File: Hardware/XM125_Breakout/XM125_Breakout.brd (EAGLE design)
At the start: 25.4 x 50.8 mm, 82 parts, among them J2 QWIIC_RIGHT_ANGLE, J3 QWIIC_RIGHT_ANGLE, U1 XM125, U2 RT9080-33GJ5, U3 RT9080-18GJ5, U4 CH340C, U5 ESD Diode

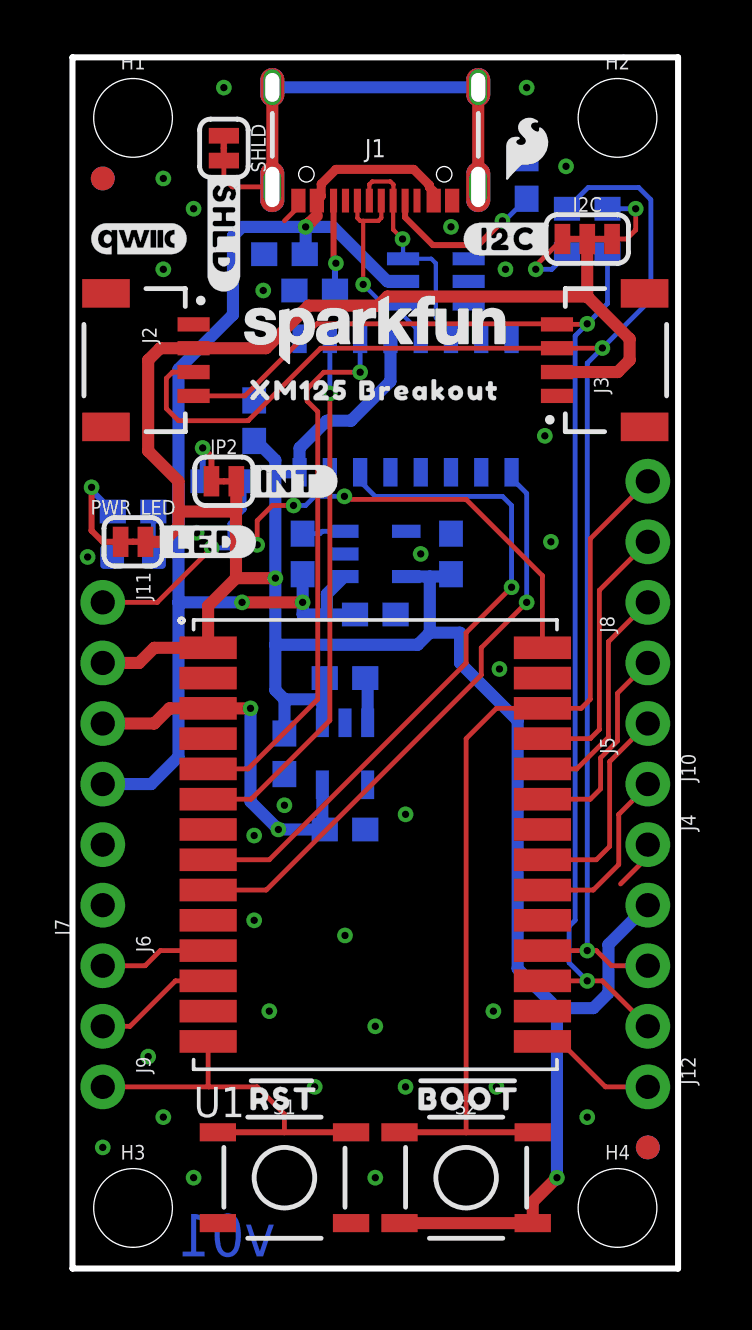
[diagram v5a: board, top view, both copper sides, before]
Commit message: Changes from design review
Final changes made - ready for re-review one last time before ordering protos
For full list of changes, see Protos Review document
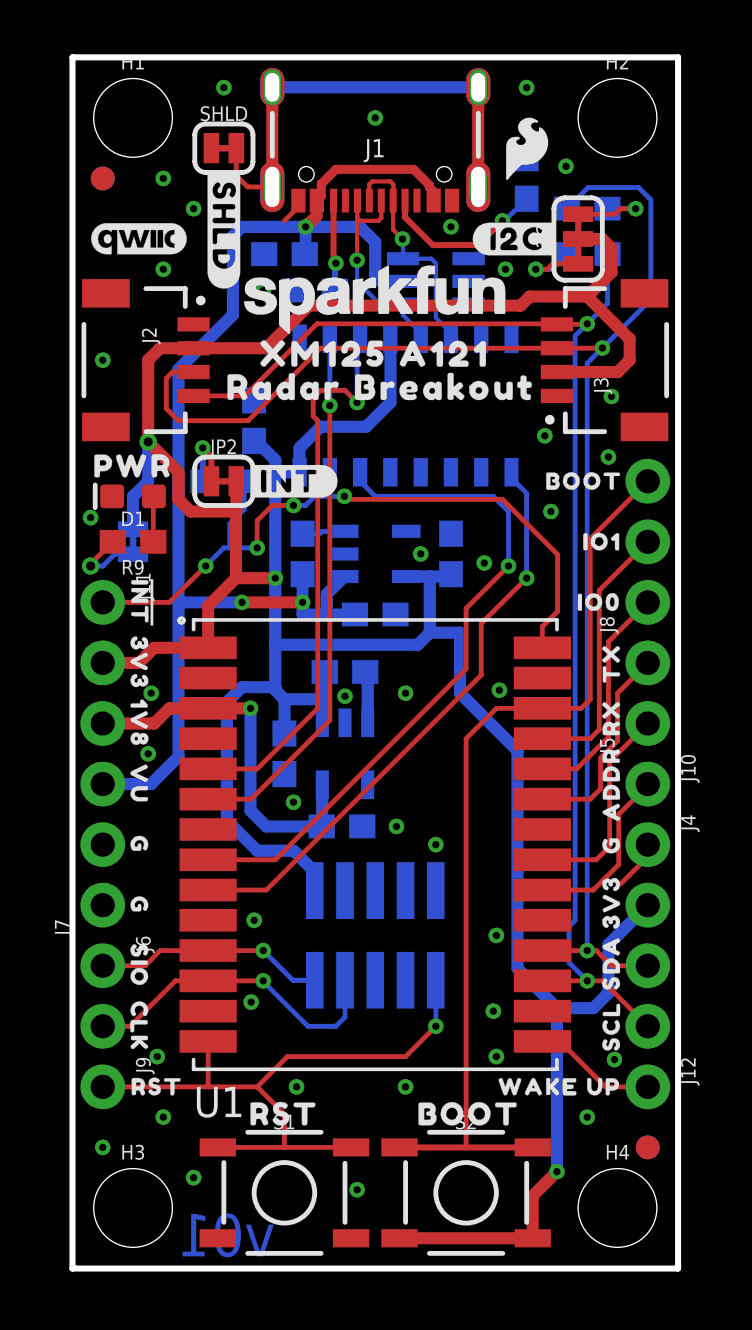
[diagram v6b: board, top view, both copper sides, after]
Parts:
- removed U$19: (no value), output:#DEBUG_RX#3
- removed U$25: (no value), output:XM125_BREAKOUT0
- removed U$60: (no value), output:#GND#17
- added J13: SWD (DNP), SparkFun-Connectors:2X5-SMD-UNSHROUDED_DNP_NO_PASTE
- added U$22: (no value), output:##RESET#136
- added U$30, U$31: (no value), output:#GND#141
- added U$32: (no value), output:#3V3#141
- added U$33: (no value), output:3V3144
- added U$34, U$35, U$36: (no value), output:G144
- added U$37: (no value), output:RST145
- added U$38: (no value), output:VU146
- added U$39: (no value), output:IO0147
- added U$40: (no value), output:IO1148
- added U$41: (no value), output:BOOT1149
- added U$42: (no value), output:CLK1150
- added U$43: (no value), output:#SWDCLK#1151
- added U$44: (no value), output:TX1153
- added U$45: (no value), output:ADDR1154
- added U$46: (no value), output:SDA1155
- added U$47: (no value), output:SCL1157
- added U$49: (no value), output:SIO1159
- added U$50: (no value), output:#WAKE_UP#1160
- added U$51: (no value), output:#DEBUG_RX#1162
- added U$52: (no value), output:#I2C_ADDR#1163
- added U$53: (no value), output:RADAR_BREAKOUT1166
- added U$54: (no value), output:XM125_A1211167
- J2, J3: value QWIIC_RIGHT_ANGLE -> RIGHT_ANGLE
- U$1: device output:#GND#17 -> output:#INT143
- U$14: device output:#3V3#10 -> output:3V3144
- U$15: device output:#GND#10 -> output:1V8144
- U$16: device output:#3V3#18 -> output:#1V8#141
- U$17: device output:#I2C_ADDR#11 -> output:RADAR_BREAKOUT1163
- U$18: device output:#DEBUG_TX#0 -> output:WAKE_UP5
- U$2: device output:#VUSB#5 -> output:##INT#2
- U$23: device output:#IO2##BOOT#134 -> output:#3V3#141
- U$24: device output:XM125_BREAKOUT127 -> output:XM125_A1211163
- U$27: device output:#LED#127 -> output:#GPIO2##BOOT#141
- U$3: device output:#INT#2 -> output:#LED#139
- U$4: device output:#1V8#3 -> output:#GND#141
- U$6: device output:#SWDIO#4 -> output:RX1152
- U$7: device output:#CLK#5 -> output:#SWDIO#4
- U$8: device output:#RESET#6 -> output:#VUSB#1
- U$9: device output:#WAKE_UP#7 -> output:#DEBUG_TX#1161
- moved LOGO4 38.1 mm to (12.7, 48.3)
- moved U$24 34.3 mm to (12.7, 2.54), flipped to the bottom
- moved U$14 21.3 mm to (2.79, 25.4), flipped to the top, turned to 270 degrees
- moved U$6 20.5 mm to (22.6, 23.1), flipped to the top, turned to 90 degrees
- moved U$27 20.4 mm to (24.1, 39.0), flipped to the bottom, turned to 90 degrees
- moved U$17 20.2 mm to (12.4, 1.27)
- moved U$15 19.3 mm to (2.79, 22.9), flipped to the top, turned to 270 degrees
- moved U$18 17.9 mm to (20.4, 7.62), flipped to the top
- moved U$9 17.8 mm to (19.2, 25.4)
- moved U$23 16.5 mm to (3.94, 25.4)
- moved U$1 12.7 mm to (2.92, 27.9), flipped to the top, turned to 270 degrees
- moved U$8 12.7 mm to (4.45, 20.3)
- moved LOGO3 11.4 mm to (12.7, 5.08)
- moved U$2 7.66 mm to (3.68, 27.9)
- moved U$4 5.08 mm to (3.94, 17.8)
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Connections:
- net XM125_INT renamed !XM125_INT
- removed net XM125_RESET: J9.1, S1.1, S1.2, U1.14
- new net !XM125_RESET: J13.10, J9.1, S1.1, S1.2, U1.14
- net 3.3V: now also J13.1
- net GND: now also J13.3, J13.5, J13.9
- net SWD_CLK: now also J13.4
- net SWD_IO: now also J13.2
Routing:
- net !XM125_RESET: track 0.00 -> 27.5 mm, vias 0 -> 1
- net 3.3V: track 130.6 -> 147.6 mm, vias 2 -> 3
- net XM125_RESET: track 16.4 -> 0.00 mm
- net SWD_CLK: track 5.21 -> 13.5 mm, vias 0 -> 1
- net SWD_IO: track 4.68 -> 9.67 mm, vias 0 -> 1
- net !XM125_INT: track 28.3 -> 29.8 mm
- net N$14: track 4.61 -> 3.38 mm
- net V_USB: track 54.7 -> 55.5 mm
- net CH340-RX: track 22.9 -> 23.7 mm
- net XM125_GPIO2/BOOT0: track 38.1 -> 38.8 mm
- net 1.8V: track 15.9 -> 15.8 mm, vias 2 -> 1
- net GND: vias 32 -> 39
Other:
- board text added: "Units: inches"

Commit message: Production files added
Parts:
- removed U$22: (no value), output:##RESET#136
- removed U$50: (no value), output:#WAKE_UP#1160
- removed U$51: (no value), output:#DEBUG_RX#1162
- removed U$52: (no value), output:#I2C_ADDR#1163
- removed U$9: (no value), output:#DEBUG_TX#1161
- added U$19: (no value), output:#RST6
- added U$25: (no value), output:##INT#8
- added U$48: (no value), output:#I2C_ADDR#12
- added U$55: (no value), output:#WAKE_UP#12
- added U$56: (no value), output:##RESET#13
- LOGO6: value SFE_LOGO_NAME.1_INCH -> SFE_LOGO_NAME_FLAME.1_INCH; device SparkFun-Aesthetics:SFE_LOGO_NAME_.1 -> SparkFun-Aesthetics:SFE_LOGO_NAME_FLAME_.1
- U$18: device output:WAKE_UP5 -> output:WU9
- U$28: device output:#INT#128 -> output:#DEBUG_TX#10
- U$37: device output:RST145 -> output:#DEBUG_RX#11
- moved U$37 21.6 mm to (18.8, 22.9), flipped to the bottom
- moved U$28 12.3 mm to (18.8, 25.4), flipped to the bottom
- moved U$18 2.16 mm to (22.6, 7.62), turned to 270 degrees
- moved LOGO6 1.27 mm to (12.7, 39.4)
- moved U$53 1.27 mm to (13.0, 35.7)
- moved U$54 1.27 mm to (12.7, 37.1)
- moved U$41 1.14 mm to (22.6, 33.0), turned to 270 degrees
- moved U$39 0.51 mm to (22.6, 27.9), turned to 270 degrees
- moved U$40 0.46 mm to (22.6, 30.2), turned to 270 degrees
- moved U$6 0.25 mm to (22.6, 22.9), turned to 270 degrees
- moved U$34 0.13 mm to (22.6, 17.7), turned to 270 degrees
- moved U$46 0.13 mm to (22.6, 12.7), turned to 270 degrees
- moved U$47 0.13 mm to (22.6, 10.0), turned to 270 degrees
- moved U$45 0.13 mm to (22.6, 20.2), turned to 270 degrees
- turned U$33 to 270 degrees
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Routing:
- net V_USB: track 55.5 -> 54.3 mm
- net GND: vias 39 -> 38
